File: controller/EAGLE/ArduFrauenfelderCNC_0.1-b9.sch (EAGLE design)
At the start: 17 parts, among them IC1 MEGA8-P, J2 POWER_JACKPTH_LOCK, Y1 16Mhz

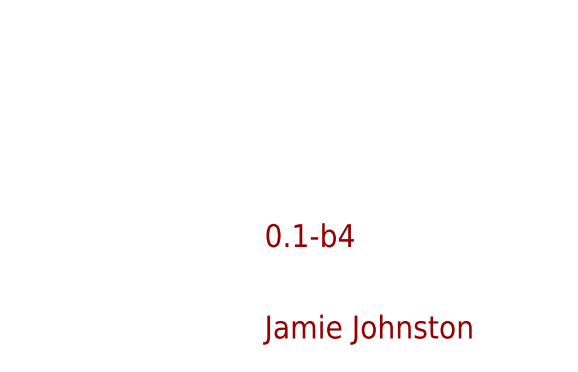
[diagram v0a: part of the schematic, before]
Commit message: Upgrade to 0.1-b9 board design.
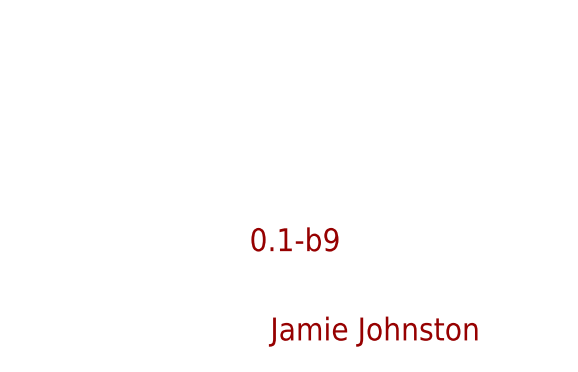
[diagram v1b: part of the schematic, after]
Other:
- note added: "0.1-b9"
- note removed: "0.1-b4"
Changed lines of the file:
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@@
 <sheet>
 <plain>
-<text x="302.26" y="-109.22" size="2.54" layer="94">Jamie Johnston</text>
-<text x="302.26" y="-99.06" size="2.54" layer="94">0.1-b4</text>
+<text x="302.90509375" y="-109.4351875" size="2.54" layer="94">Jamie Johnston</text>
+<text x="300.59325" y="-99.516825" size="2.54" layer="94">0.1-b9</text>
 </plain>
 <instances>
